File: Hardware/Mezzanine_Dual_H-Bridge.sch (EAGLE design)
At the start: 17 parts, among them U1 TB6612FNG, U2 EDISON_CONNECTOR_FULLMOUNTING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, U3 EDISON_CONNECTOR_FULLHEADER

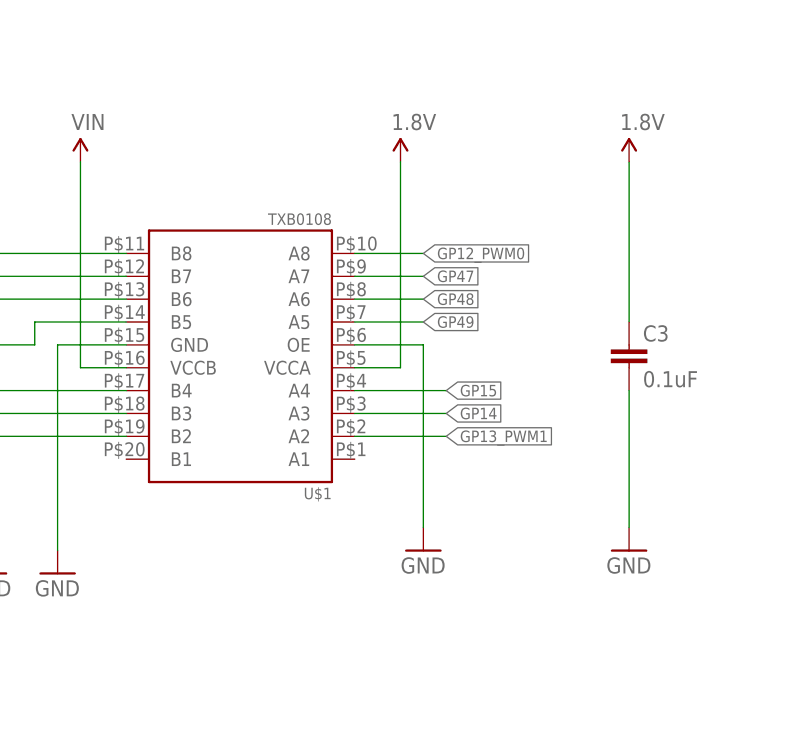
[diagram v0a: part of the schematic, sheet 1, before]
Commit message: fixed OE high
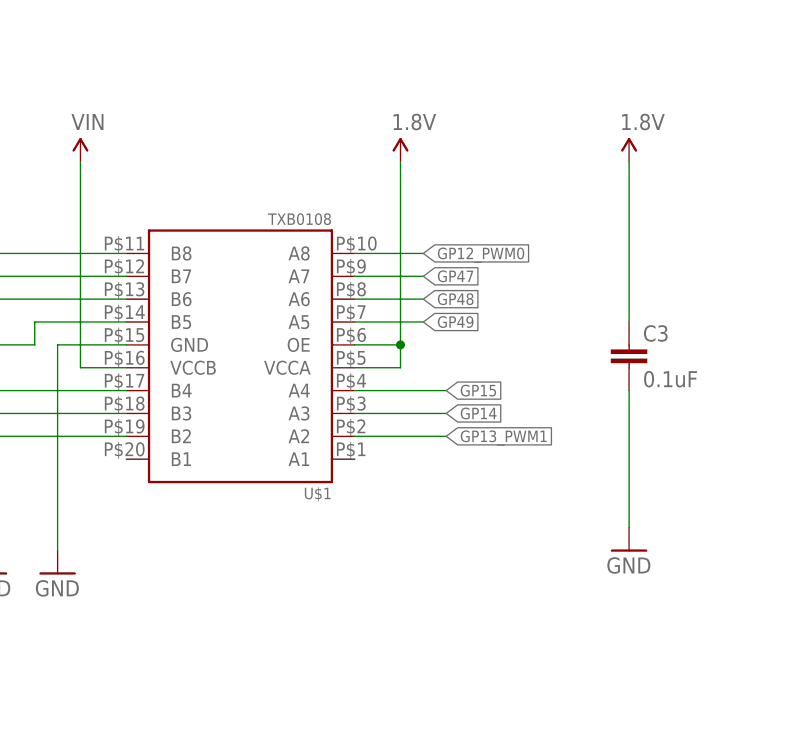
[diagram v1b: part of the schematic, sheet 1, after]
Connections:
- net 1.8V: now also U$1.OE
- net GND: no longer U$1.OE
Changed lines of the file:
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@@
 <part name="SUPPLY3" library="SparkFun-Aesthetics" deviceset="VIN" device=""/>
 <part name="SUPPLY4" library="SparkFun-Aesthetics" deviceset="1.8V" device=""/>
-<part name="GND7" library="SparkFun-Aesthetics" deviceset="GND" device=""/>
 <part name="C1" library="SparkFun-Capacitors" deviceset="10UF-16V-10%(TANT)" device="" value="10uF"/>
 <part name="C2" library="SparkFun-Capacitors" deviceset="0.1UF-25V(+80/-20%)(0603)" device="" value="0.1uF"/>
@@
 <instance part="SUPPLY3" gate="G$1" x="149.86" y="129.54"/>
 <instance part="SUPPLY4" gate="G$1" x="185.42" y="129.54"/>
-<instance part="GND7" gate="1" x="187.96" y="86.36"/>
 <instance part="C1" gate="G$1" x="48.26" y="104.14"/>
 <instance part="C2" gate="G$1" x="38.1" y="101.6"/>
@@
 </segment>
 <segment>
-<wire x1="180.34" y1="109.22" x2="187.96" y2="109.22" width="0.1524" layer="91"/>
-<wire x1="187.96" y1="109.22" x2="187.96" y2="88.9" width="0.1524" layer="91"/>
-<pinref part="GND7" gate="1" pin="GND"/>
-<pinref part="U$1" gate="G$1" pin="OE"/>
-</segment>
-<segment>
 <pinref part="C3" gate="G$1" pin="2"/>
 <pinref part="GND8" gate="1" pin="GND"/>
@@
 <segment>
 <wire x1="180.34" y1="106.68" x2="185.42" y2="106.68" width="0.1524" layer="91"/>
-<wire x1="185.42" y1="106.68" x2="185.42" y2="129.54" width="0.1524" layer="91"/>
+<wire x1="185.42" y1="106.68" x2="185.42" y2="109.22" width="0.1524" layer="91"/>
 <pinref part="SUPPLY4" gate="G$1" pin="1.8V"/>
 <pinref part="U$1" gate="G$1" pin="VCCA"/>
-</segment>
-<segment>
+<pinref part="U$1" gate="G$1" pin="OE"/>
+<wire x1="185.42" y1="109.22" x2="185.42" y2="129.54" width="0.1524" layer="91"/>
+<wire x1="180.34" y1="109.22" x2="185.42" y2="109.22" width="0.1524" layer="91"/>
+<junction x="185.42" y="109.22"/>
+</segment>
+<segment>

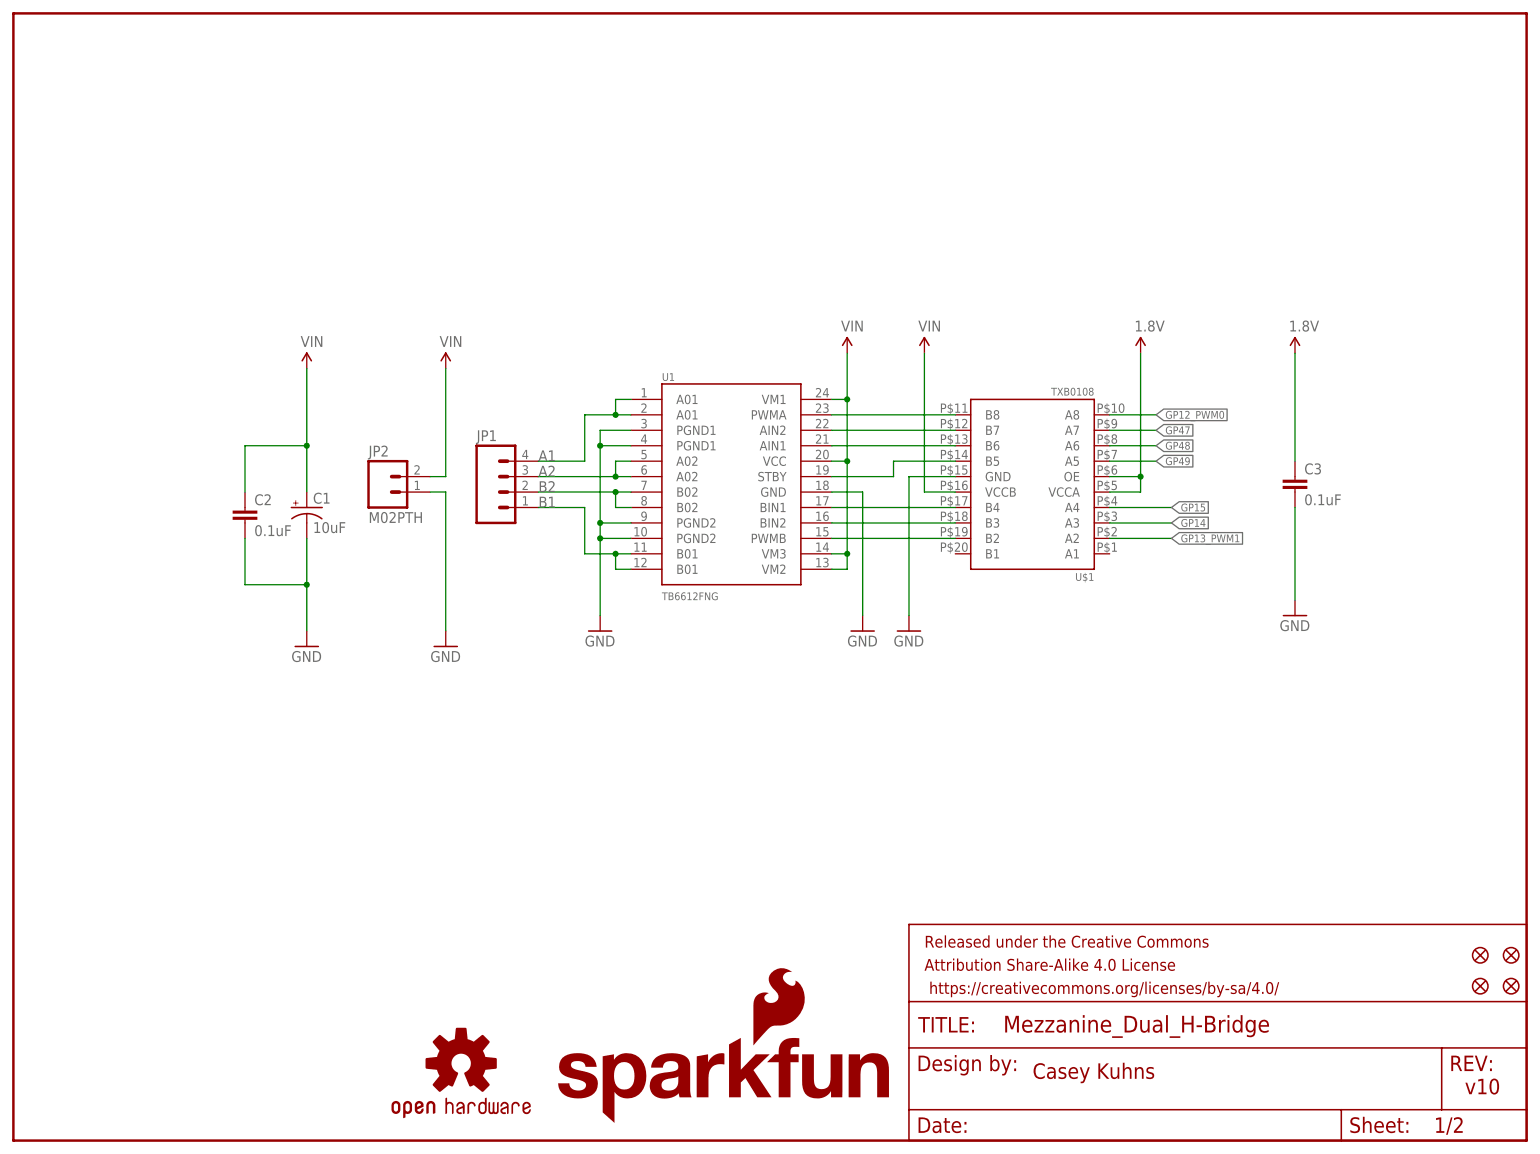
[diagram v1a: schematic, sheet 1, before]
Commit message: Added LED's for motor direction Added Diode Jumper circuit to enable VSYS to power VIN Corrected Name and location Removed extra dimensions and cleaned up drawing Added DCIN pin and completed circuit.
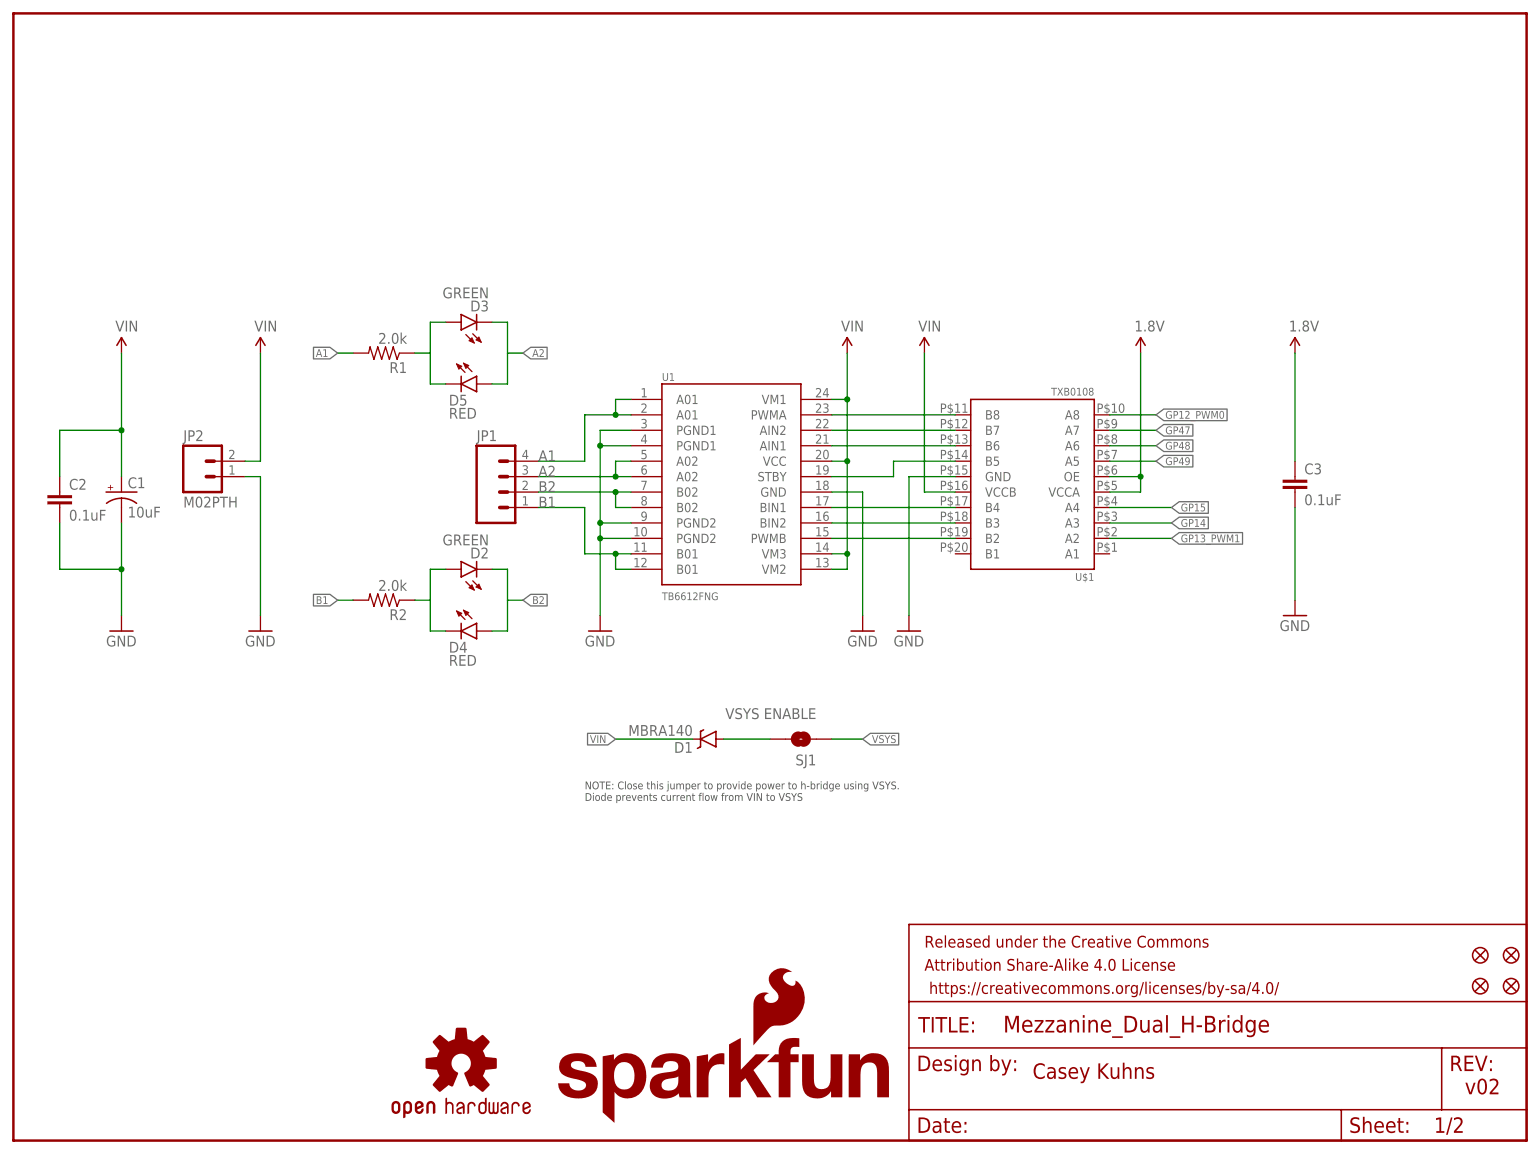
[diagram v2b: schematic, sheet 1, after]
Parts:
- added D1: MBRA140, SparkFun-DiscreteSemi:DIODE-SCHOTTKY-MBRA140
- added D2, D3: GREEN, SparkFun-LED:LED-GREEN0603
- added D4, D5: RED, SparkFun-LED:LED-RED0603
- added R1, R2: 2.0k, SparkFun-Resistors:2.0KOHM1/10W5%(0603)
- added SJ1: VSYS ENABLE, SparkFun-Passives:JUMPER-PAD-2-NOYES_SILK
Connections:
- new net DCIN: U2.DCIN, U3.DCIN
- new net N$1: D1.A, SJ1.2
- new net N$2: D2.A, D4.C, R2.1
- new net N$5: D3.A, D5.C, R1.1
- net A1: now also R1.2
- net A2: now also D3.C, D5.A
- net B1: now also R2.2
- net B2: now also D2.C, D4.A
- net VIN: now also D1.C
- net VSYS: now also SJ1.1
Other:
- note added: "NOTE: Close this jumper to provide power to h-bridge using VSYS. Diode prevents current flow from VIN to VSYS"
- note added: "v02"
- note removed: "v10"
- moved on the sheet: C1, C2, JP2
